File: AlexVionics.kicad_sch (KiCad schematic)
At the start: 0 parts

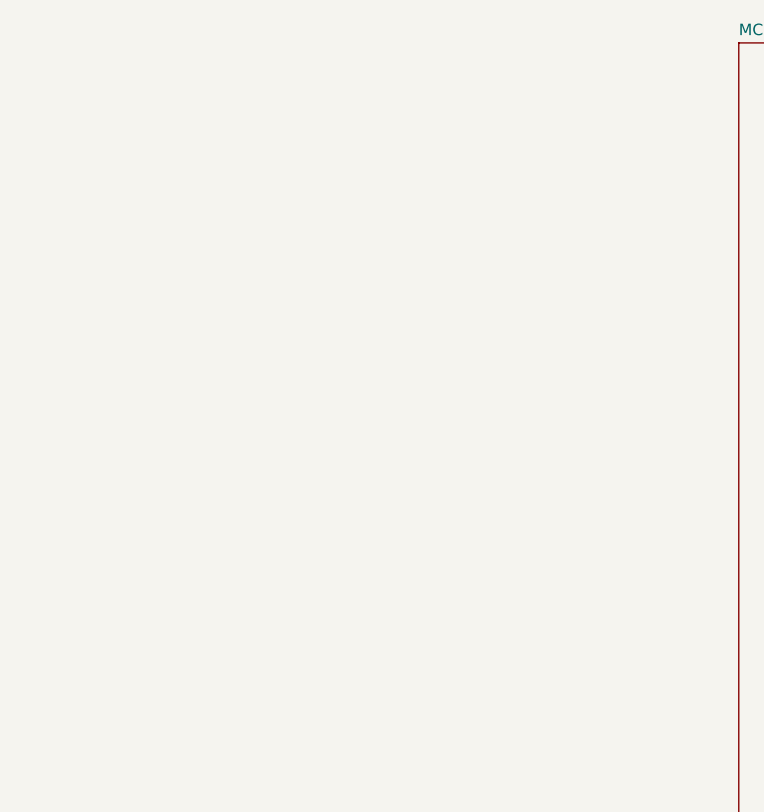
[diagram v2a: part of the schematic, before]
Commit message: fixed symbol table and created POWER
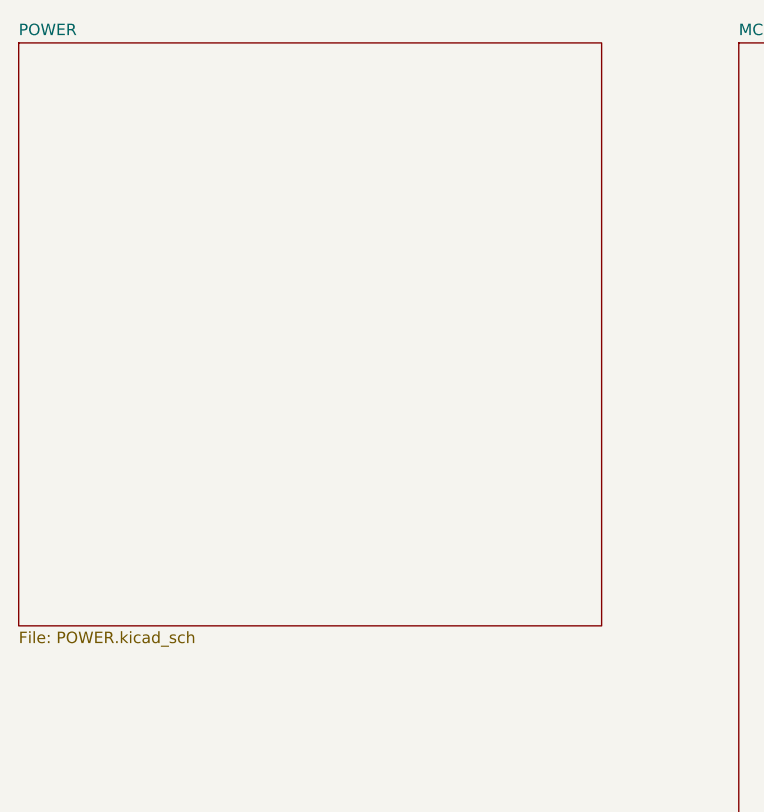
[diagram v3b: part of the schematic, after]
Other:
- added sheet POWER (POWER.kicad_sch)
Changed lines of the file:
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@@
+    )
+  )
+  (sheet (at 22.86 22.86) (size 64.77 64.77) (fields_autoplaced)
+    (stroke (width 0.1524) (type solid) (color 0 0 0 0))
+    (fill (color 0 0 0 0.0000))
+    (property "Sheet name" "POWER" (id 0) (at 22.86 22.1484 0)
+      (effects (font (size 1.27 1.27)) (justify left bottom))
+    )
+    (property "Sheet file" "POWER.kicad_sch" (id 1) (at 22.86 88.2146 0)
+      (effects (font (size 1.27 1.27)) (justify left top))
     )
   )
@@
     (path "/bc2005ae-598d-43fd-8610-1af53ee6d8a1" (page "3"))
     (path "/2fc0ce4a-f513-44b9-bde6-b00ebdd65969" (page "4"))
+    (path "/389aefcf-b314-4aab-b5ae-32c0773405d5" (page "5"))
   )
   (symbol_instances

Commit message: started connecting board
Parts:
- added J?: USB_C_Receptacle_USB2.0, symbol Connector:USB_C_Receptacle_USB2.0
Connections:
- new net: J?.A1 (GND), J?.A12 (GND), J?.B1 (GND), J?.B12 (GND)
- new net VBUS: J?.A4 (VBUS), J?.A9 (VBUS), J?.B4 (VBUS), J?.B9 (VBUS)
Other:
- sheet MCU ports: added A0, A1, A2, A3, GPIO10, GPIO11, GPIO2, GPIO21, GPIO22, GPIO23, GPIO24, GPIO25, GPIO3, GPIO4, GPIO5, GPIO6, GPIO7, GPIO8, GPIO9, I2C0_SCL, I2C0_SDA, RESET, SPI0_SCK, SPI0_SDI, SPI0_SDO, UART0_RX, UART0_TX, USB_BOOT, USB_DM, USB_DP; removed none
- sheet SENSORS ports: added LIS2_CS, LSM6_CS, LSM6_INT1, LSM6_INT2, MS5611_CS, SNS_SPI_MISO, SNS_SPI_MOSI, SNS_SPI_SCK; removed none
- sheet TELEMETRY ports: added 1HZ, GPS_RESET, GPS_RX, GPS_SAFEBOOT, GPS_SCL, GPS_SDA, GPS_TX, RFM96W_CS, RFM96W_DIO0, RFM96W_DIO1, RFM96W_DIO2, RFM96W_DIO3, RFM96W_DIO4, RFM96W_DIO5, RFM96W_RESET, RFM96W_SCK, RFM96W_SDI, RFM96W_SDO; removed none

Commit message: finished routing
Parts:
- added D101: GREEN, LED_SMD:LED_0603_1608Metric, symbol Device:LED
- added D102: WHITE, LED_SMD:LED_0603_1608Metric, symbol Device:LED
- added D103: BLUE, LED_SMD:LED_0603_1608Metric, symbol Device:LED
- added R101, R103: 5.1k, Resistor_SMD:R_0402_1005Metric, symbol Device:R_US
- added R102, R104, R105: 470, Resistor_SMD:R_0402_1005Metric, symbol Device:R_US
- added SW101, SW102, SW103: PTS636, Button_Switch_SMD:SW_SPST_FSMSM, symbol Switch:SW_Push
- J101: renamed from J?; footprint (none) -> Connector_USB:USB_C_Receptacle_Amphenol_12401610E4-2A
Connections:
- net MCU/GPIO21: now also D103.2 (A)
- net MCU/GPIO22: now also D101.2 (A)
- net MCU/GPIO23: now also SW101.2
- net MCU/RESET: now also SW103.2
- net MCU/USB_BOOT: now also SW102.2
- net MCU/USB_DM: now also J101.A7 (D-), J101.B7 (D-)
- net MCU/USB_DP: now also J101.A6 (D+), J101.B6 (D+)
- net GND: now reaches J101.A1 (GND), J101.A12 (GND), J101.B1 (GND), J101.B12 (GND)
- net GND: now also J101.S1 (SHIELD), R101.2, R102.1, R103.2, R104.1, R105.1, SW101.1, SW102.1, SW103.1
- net at J101.A5 (CC1): now also R101.1
- net at J101.B5 (CC2): now also R103.1
- new net: D102.1 (K), R105.2
- new net: D103.1 (K), R104.2
- new net: D101.1 (K), R102.2
- new net +3V3: D102.2 (A)
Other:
- sheet MCU ports: added none; removed GPIO10, GPIO11
- sheet POWER ports: added BATT_VOLTAGE_MONITOR; removed none
- moved on the sheet: J101
